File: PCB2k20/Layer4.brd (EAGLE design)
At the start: 160 x 100 mm, 32 parts

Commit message: Layer 4: linked with fusion so its easier to move stuff around
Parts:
- removed 1R2: 1k, JH:R0603
- removed 1R3: 10k, JH:R0603
- removed 1S1: 34-MOMENTARY-SWITCH, JH:3*4-MOMENTARY-SWITCH
- added J1, J2: CONN_03, JH:1X03_LOCK
- added J3: (no value), SparkFun-Connectors:1X05_LOCK
- added R1: 10k, JH:R0603
- added U$1: 74HCT08, JH:SOIC-14
- 1S2: value 34-MOMENTARY-SWITCH -> MOMENTARY_SWITCH_4X3; device JH:3*4-MOMENTARY-SWITCH -> JH:MOMENTARY_SWITCH_4X3
- D1, D10, D11, D12, D13, D14, D15, D16, D2, D3, D4, D5, D6, D7, D8, D9: device SparkFun-LED:WS2812B -> JH:WS2812B
- moved D15 82.0 mm to (24.9, -24.9), turned to 315 degrees
- moved D14 76.7 mm to (13.5, -32.6), turned to 292.5 degrees
- moved D16 74.0 mm to (32.6, -13.5), turned to 337.5 degrees
- moved D13 71.5 mm to (0.00, -35.2), turned to 270 degrees
- moved D12 62.0 mm to (-13.5, -32.6), turned to 247.5 degrees
- moved D3 60.5 mm to (24.9, 24.9), turned to 45 degrees
- moved 1C8 59.9 mm to (-88.9, -36.8)
- moved 1D1 59.9 mm to (-88.9, -44.5)
- moved 1C11 59.9 mm to (-77.5, -36.8)
- moved 1C3 59.9 mm to (-73.7, -33.0)
- moved 1C4 59.9 mm to (-69.8, -33.0)
- moved 1OSC 59.9 mm to (-91.4, -20.3)
- moved 1R1 59.9 mm to (-73.7, -36.8)
- moved 1R4 59.9 mm to (-62.2, -36.8)
- moved 1S2 59.9 mm to (-68.6, -20.3)
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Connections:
- net 15 renamed SDA
- net 16 renamed SCL
- net 17 renamed TOF3_XSHUT
- net 18 renamed TOF3_GPIO
- net 19 renamed TOF4_XSHUT
- net 20 renamed TOF4_GPIO
- net 28 renamed TOF1_XSHUT
- net 29 renamed TOF1_GPIO
- net 30 renamed TOF2_XSHUT
- net 31 renamed TOF2_GPIO
- removed net 0: 1U1.22
- removed net 1: 1U1.21
- removed net 10: 1U1.11
- removed net 11: 1U1.10
- removed net 12: 1U1.4
- removed net 13: 1U1.3
- removed net 14: 1U1.2
- removed net 2: 1U1.20
- removed net 23_USBDP: 1U1.33
- removed net 24_USBDM: 1U1.32
- removed net 25: 1U1.31
- removed net 26: 1U1.30
- removed net 27: 1U1.29
- removed net 3: 1U1.18
- removed net 32: 1R3.2, 1S1.P2, 1U1.44, 1U1.45
- removed net 4: 1U1.17
- removed net 5: 1U1.16
- removed net 6: 1U1.15
- removed net 7: 1U1.14
- removed net 8: 1U1.13
- removed net 9: 1U1.12
- removed net DISC: 1U1.46
- removed net N$1: 1R2.1, 1S1.P1
- new net 5V: J3.5, U$1.P10, U$1.P14, U$1.P2, U$1.P5
- new net ESC1_IN: 1U1.29, U$1.P4
- new net ESC1_OUT: J1.3, U$1.P6
- new net ESC2_IN: 1U1.11, U$1.P9
- new net ESC2_OUT: J2.3, U$1.P8
- new net N$23: 1U1.44, R1.1
- new net USART1_RX: 1U1.31, J3.3
- new net USART1_TX: 1U1.30, J3.2
- new net WS2812B: 1U1.17, U$1.P1
- new net WS2812B_OUT: D1.4, U$1.P3
- net 3.3V: now also J3.4; no longer 1R2.2
- net GND: now also J1.1, J2.1, J3.1, R1.2, U$1.P7; no longer 1R3.1
- net N$4: now also 1S2.P$1; no longer 1S2.P1
- net RESET: now also 1S2.P$2; no longer 1S2.P2
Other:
- board size 160 x 100 mm -> 94 x 94 mm

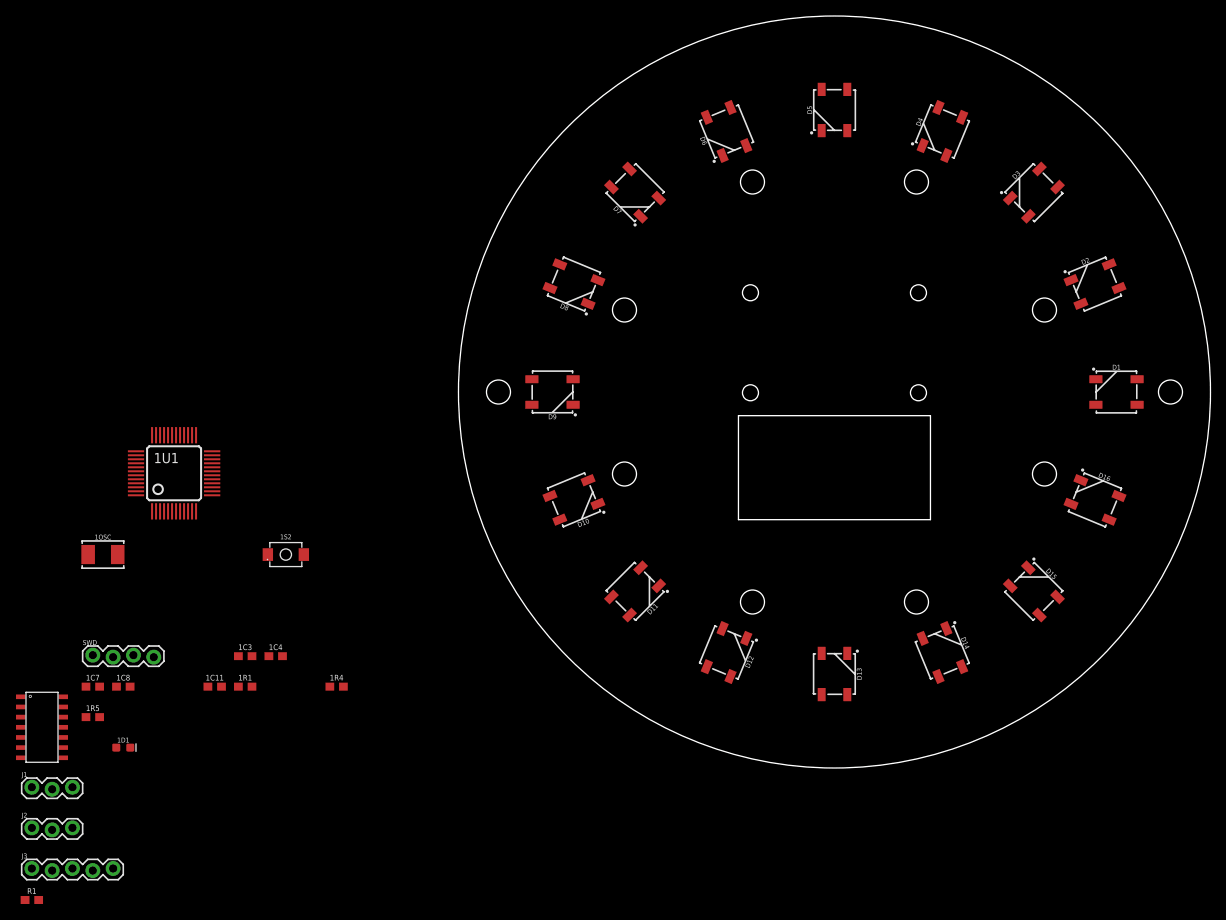
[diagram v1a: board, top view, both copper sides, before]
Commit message: finish layer 4 and start on layer 3, TODO: silkscreen for layer4
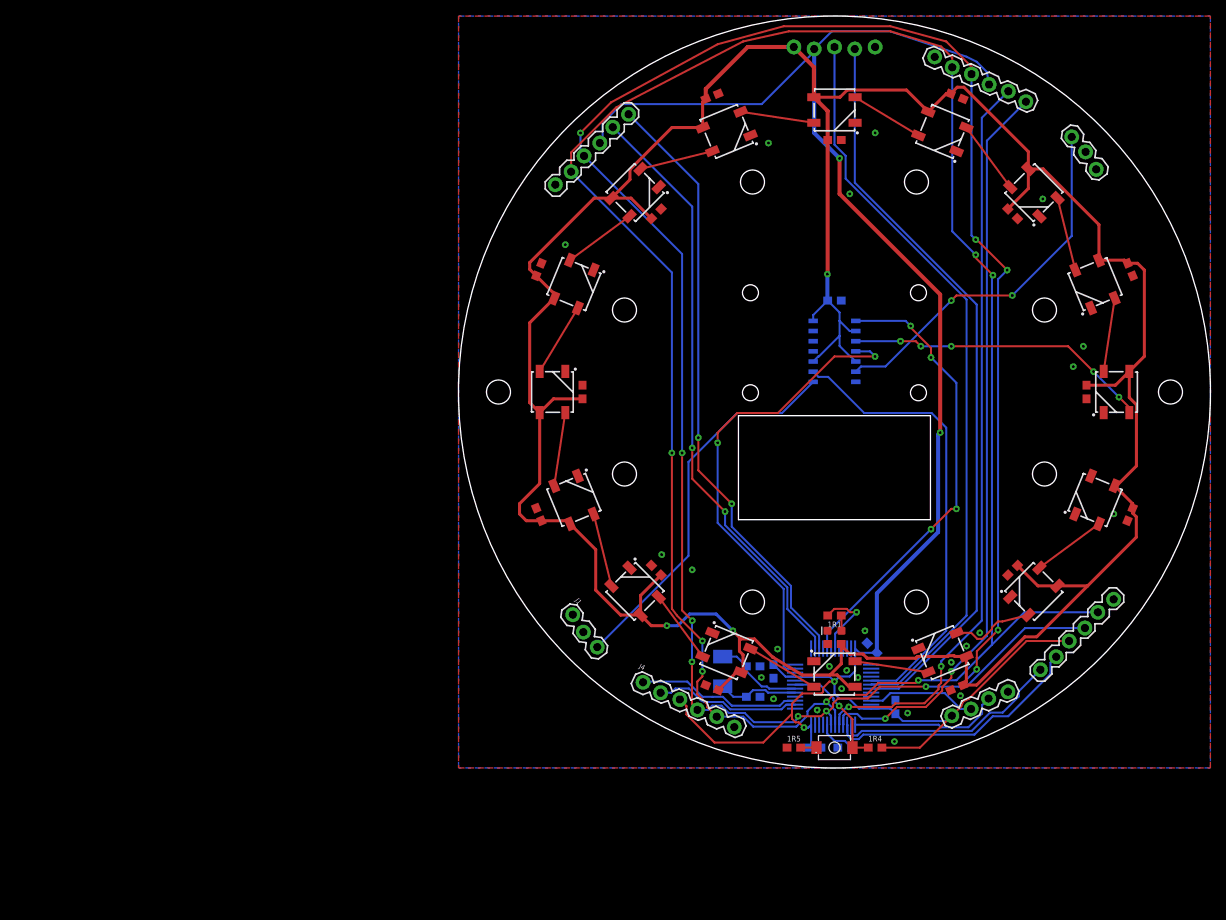
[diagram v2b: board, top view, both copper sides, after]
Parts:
- added 1C1: 1uF, JH:C0603
- added 1C2, AC1, AC2, AC3, AC4, AC5, AC6, AC7, AC8, C1, C11, C13, C15, C3, C5, C7, C9: 0.1uF, JH:C0603
- added J4, J5, J6, J7: (no value), SparkFun-Connectors:1X06_LOCK
- moved J2 156.6 mm to (32.8, 27.9), turned to 127 degrees
- moved J3 147.2 mm to (5.08, 43.0), flipped to the bottom
- moved SWD 114.4 mm to (21.6, -37.4), turned to 205 degrees
- moved U$1 109.6 mm to (0.00, 5.08), flipped to the bottom
- moved R1 103.4 mm to (1.27, -44.5), flipped to the bottom
- moved 1D1 90.1 mm to (0.00, -29.8), turned to 180 degrees
- moved 1R5 87.7 mm to (-5.08, -44.5)
- moved 1U1 86.6 mm to (-0.17, -36.8), flipped to the bottom, turned to 90 degrees
- moved 1C7 82.6 mm to (-10.2, -38.1), flipped to the bottom, turned to 180 degrees
- moved 1C3 81.5 mm to (7.62, -39.4), flipped to the bottom, turned to 90 degrees
- moved 1OSC 78.8 mm to (-14.0, -34.9), flipped to the bottom, turned to 90 degrees
- moved 1C8 78.8 mm to (-10.2, -34.3), flipped to the bottom, turned to 180 degrees
- moved 1C11 75.3 mm to (-2.54, -44.5), flipped to the bottom, turned to 180 degrees
- moved 1C4 74.6 mm to (4.70, -32.0), flipped to the bottom, turned to 45 degrees
- moved 1R1 74.2 mm to (0.00, -27.9), turned to 180 degrees
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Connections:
- net 3.3V: now also 1C1.1, J4.3, J5.4, J6.3, J7.4; no longer D1.1, D10.1, D11.1, D12.1, D13.1, D14.1, D15.1, D16.1, D2.1, D3.1, D4.1, D5.1, D6.1, D7.1, D8.1, D9.1
- net 5V: now also 1C2.1, AC1.1, AC2.1, AC3.1, AC4.1, AC5.1, AC6.1, AC7.1, AC8.1, C1.1, C11.1, C13.1, C15.1, C3.1, C5.1, C7.1, C9.1, D1.1, D10.1, D11.1, D12.1, D13.1, D14.1, D15.1, D16.1, D2.1, D3.1, D4.1, D5.1, D6.1, D7.1, D8.1, D9.1
- net ESC1_IN: now also U$1.P9; no longer U$1.P4
- net ESC1_OUT: now also U$1.P8; no longer U$1.P6
- net ESC2_IN: now also U$1.P4; no longer U$1.P9
- net ESC2_OUT: now also U$1.P6; no longer U$1.P8
- net GND: now also 1C1.2, 1C2.2, AC1.2, AC2.2, AC3.2, AC4.2, AC5.2, AC6.2, AC7.2, AC8.2, C1.2, C11.2, C13.2, C15.2, C3.2, C5.2, C7.2, C9.2, J4.6, J5.1, J6.6, J7.1
- net SCL: now also J4.5, J5.2, J6.5, J7.2
- net SDA: now also J4.4, J5.3, J6.4, J7.3
- net TOF1_GPIO: now also 1U1.2, J4.2; no longer 1U1.27
- net TOF1_XSHUT: now also 1U1.3, J4.1; no longer 1U1.28
- net TOF2_GPIO: now also 1U1.14, J5.5; no longer 1U1.25
- net TOF2_XSHUT: now also 1U1.15, J5.6; no longer 1U1.26
- net TOF3_GPIO: now also 1U1.41, J6.2; no longer 1U1.40
- net TOF3_XSHUT: now also 1U1.40, J6.1; no longer 1U1.41
- net TOF4_GPIO: now also 1U1.39, J7.5; no longer 1U1.38
- net TOF4_XSHUT: now also 1U1.38, J7.6; no longer 1U1.39
- net USART1_RX: now also J3.2; no longer J3.3
- net USART1_TX: now also J3.3; no longer J3.2
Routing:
- net 5V: track 0.00 -> 387.6 mm, vias 0 -> 3
- net SDA: track 0.00 -> 271.0 mm, vias 0 -> 11
- net SCL: track 0.00 -> 264.8 mm, vias 0 -> 7
- net 3.3V: track 0.00 -> 240.7 mm, vias 0 -> 4
- net USART1_RX: track 0.00 -> 93.7 mm
- net USART1_TX: track 0.00 -> 93.4 mm
- net TOF3_GPIO: track 0.00 -> 93.4 mm, vias 0 -> 2
- net TOF3_XSHUT: track 0.00 -> 93.2 mm, vias 0 -> 2
- net TOF2_XSHUT: track 0.00 -> 76.7 mm, vias 0 -> 2
- net TOF2_GPIO: track 0.00 -> 75.6 mm, vias 0 -> 2
- net ESC2_IN: track 0.00 -> 60.5 mm, vias 0 -> 2
- net WS2812B: track 0.00 -> 56.9 mm, vias 0 -> 4
- net ESC1_IN: track 0.00 -> 56.9 mm
- net ESC1_OUT: track 0.00 -> 47.6 mm
- net ESC2_OUT: track 0.00 -> 46.4 mm, vias 0 -> 2
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- added copper zone on layer 1, net GND
- added copper zone on layer 16, net GND

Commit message: done just need to silkscreen now!!!
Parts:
- added S1: (no value), SparkFun-Switches:SWITCH_SPDT_PTH_11.6X4.0MM_LOCK
- SWD: value (none) -> SM06B-SRSS-TB; device SparkFun-Connectors:1X04_LOCK -> con-JST SH:SM06B-SRSS-TB
- moved SWD 3.81 mm to (18.2, -39.0)
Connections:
- new net DEBUG_RX: 1U1.13, SWD.6
- new net DEBUG_TX: 1U1.12, SWD.5
- new net N$26: J3.4, S1.2
- net 3.3V: now also S1.1; no longer J3.4
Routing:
- net DEBUG_TX: track 0.00 -> 39.0 mm, vias 0 -> 3
- net DEBUG_RX: track 0.00 -> 37.8 mm, vias 0 -> 3
- net N$26: track 0.00 -> 15.8 mm, vias 0 -> 1
- net SDA: track 271.0 -> 263.9 mm
- net 3.3V: track 240.7 -> 244.0 mm, vias 4 -> 6
- net 21: track 18.9 -> 16.8 mm, vias 0 -> 1
- net 22: track 13.7 -> 15.7 mm, vias 0 -> 1
- net 5V: track 387.6 -> 385.8 mm
- net USART1_TX: track 93.4 -> 92.7 mm
- net ESC1_IN: track 56.9 -> 56.1 mm
- net USART1_RX: track 93.7 -> 93.0 mm
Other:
- outline, holes or cut-outs redrawn
- board text added: "xshut"

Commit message: add gerbers, please everything turn out well!
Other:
- outline, holes or cut-outs redrawn
- board text added: "3v3"
- board text added: "5v"
- board text added: "CAMERA"
- board text added: "OFF"
- board text added: "ON"
- board text added: "gnd"
- board text added: "gpio"
- board text added: "power"
- board text added: "rx"
- board text added: "scl"
- board text added: "sda"
- board text added: "sig"
- board text added: "tx"

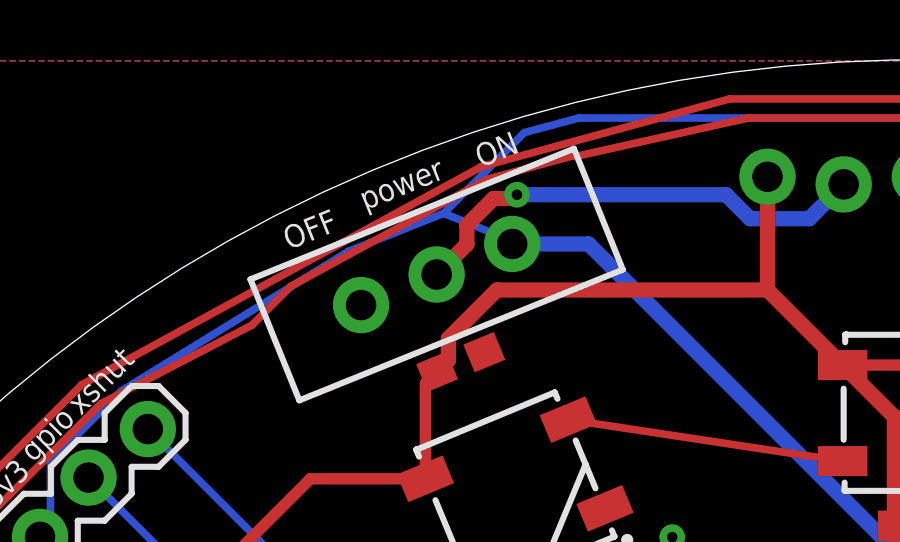
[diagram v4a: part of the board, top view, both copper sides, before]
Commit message: BROKEN VERSION for 3d models
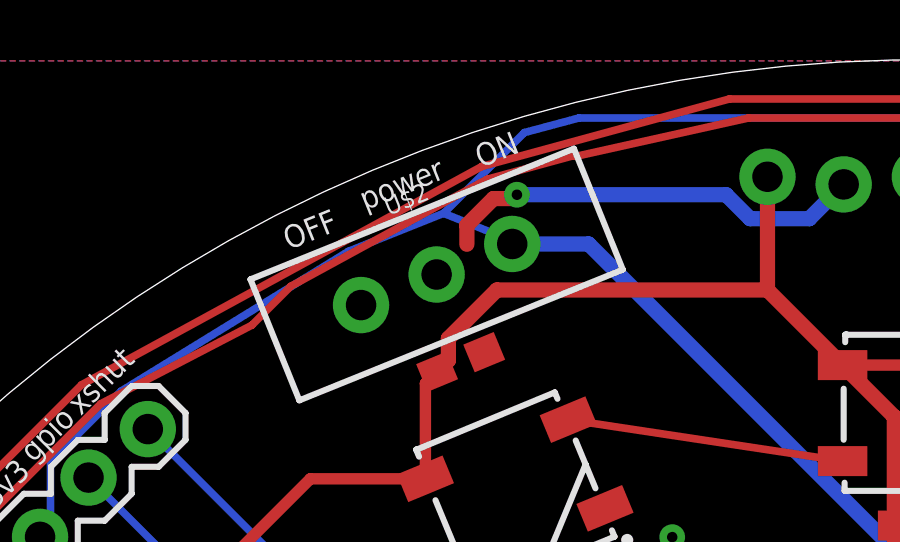
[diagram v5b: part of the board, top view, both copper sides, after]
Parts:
- removed S1: (no value), SparkFun-Switches:SWITCH_SPDT_PTH_11.6X4.0MM_LOCK
- added U$2: SWITCH_SPDT_TH, JH:SWITCH_SPDT_PTH_11.6X4.0MM_LOCK
- 1D1: device SparkFun-LED:LED-0603 -> JH:LED-0603
- 1OSC: device SparkFun-Clocks:CRYSTAL-SMD-5X3.2-2PAD -> JH:CRYSTAL-SMD-5X3.2-2PAD
- J3: device SparkFun-Connectors:1X05_LOCK -> Connectors:1X05_LOCK
- J4, J5, J6, J7: device SparkFun-Connectors:1X06_LOCK -> Connectors:1X06_LOCK
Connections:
- net 3.3V: now also U$2.1; no longer S1.1
- net N$26: now also U$2.2; no longer S1.2
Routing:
- net N$26: track 15.8 -> 14.4 mm
